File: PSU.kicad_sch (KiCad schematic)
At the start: 11 parts, among them J1 Mini USB Female, J2 Battery Connector, U3 AMS1117-3.3

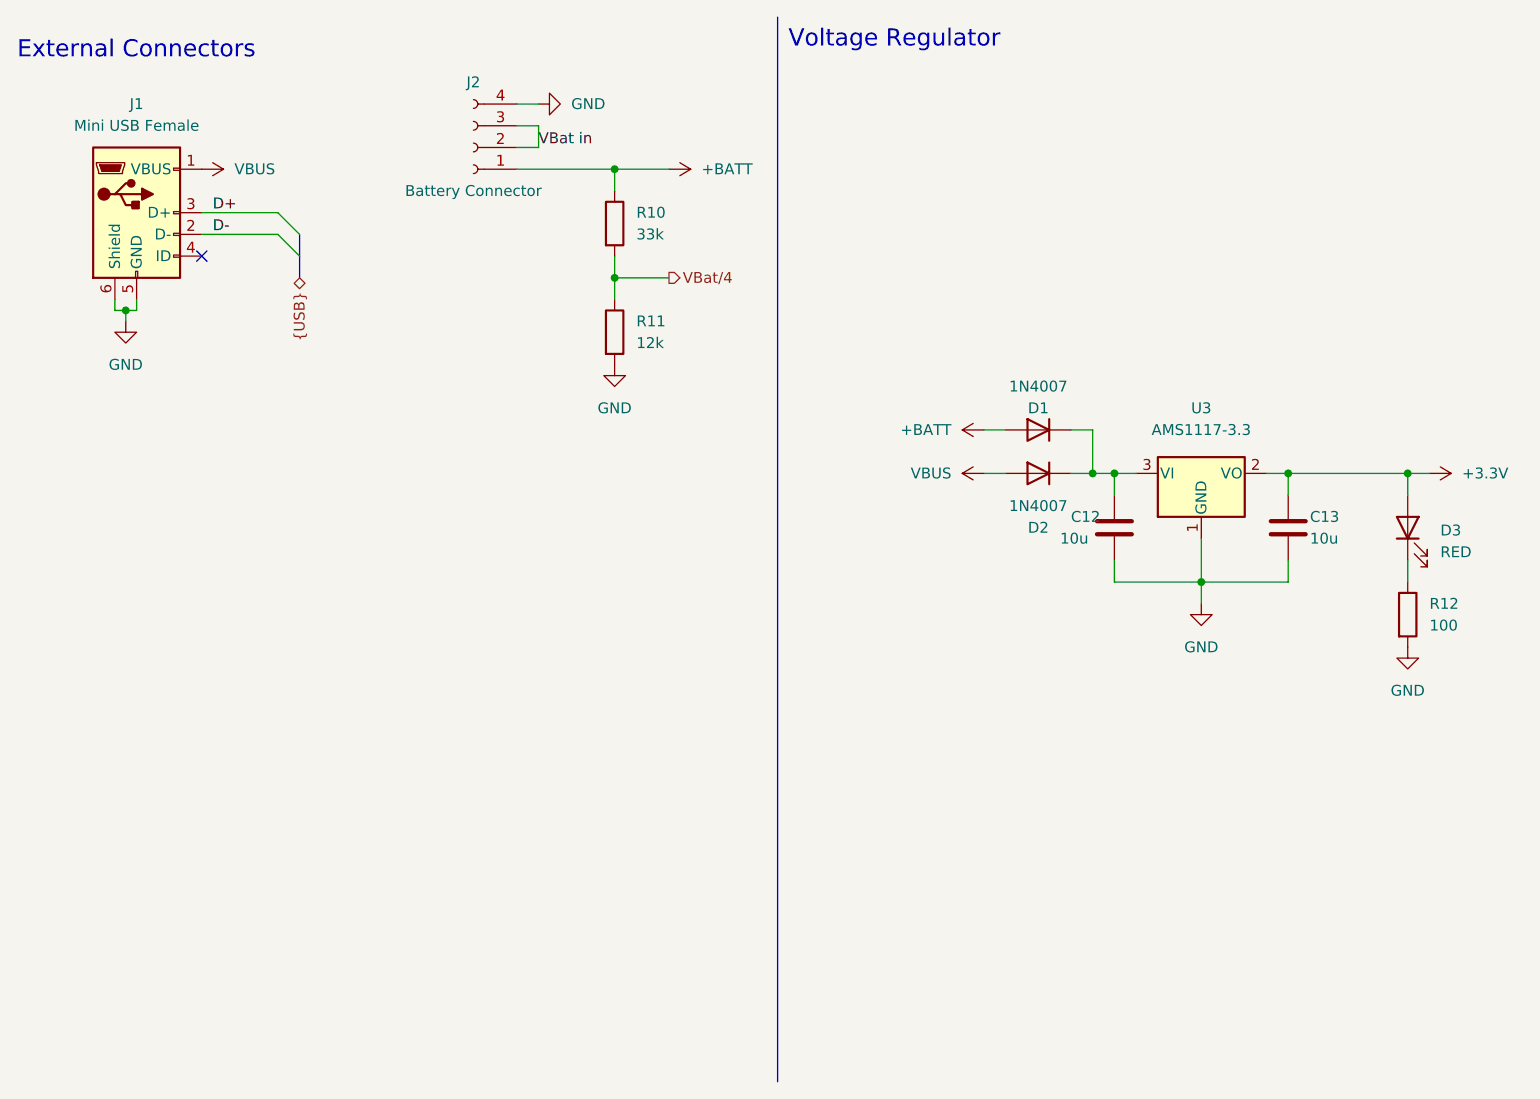
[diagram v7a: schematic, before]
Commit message: Added polyfuse
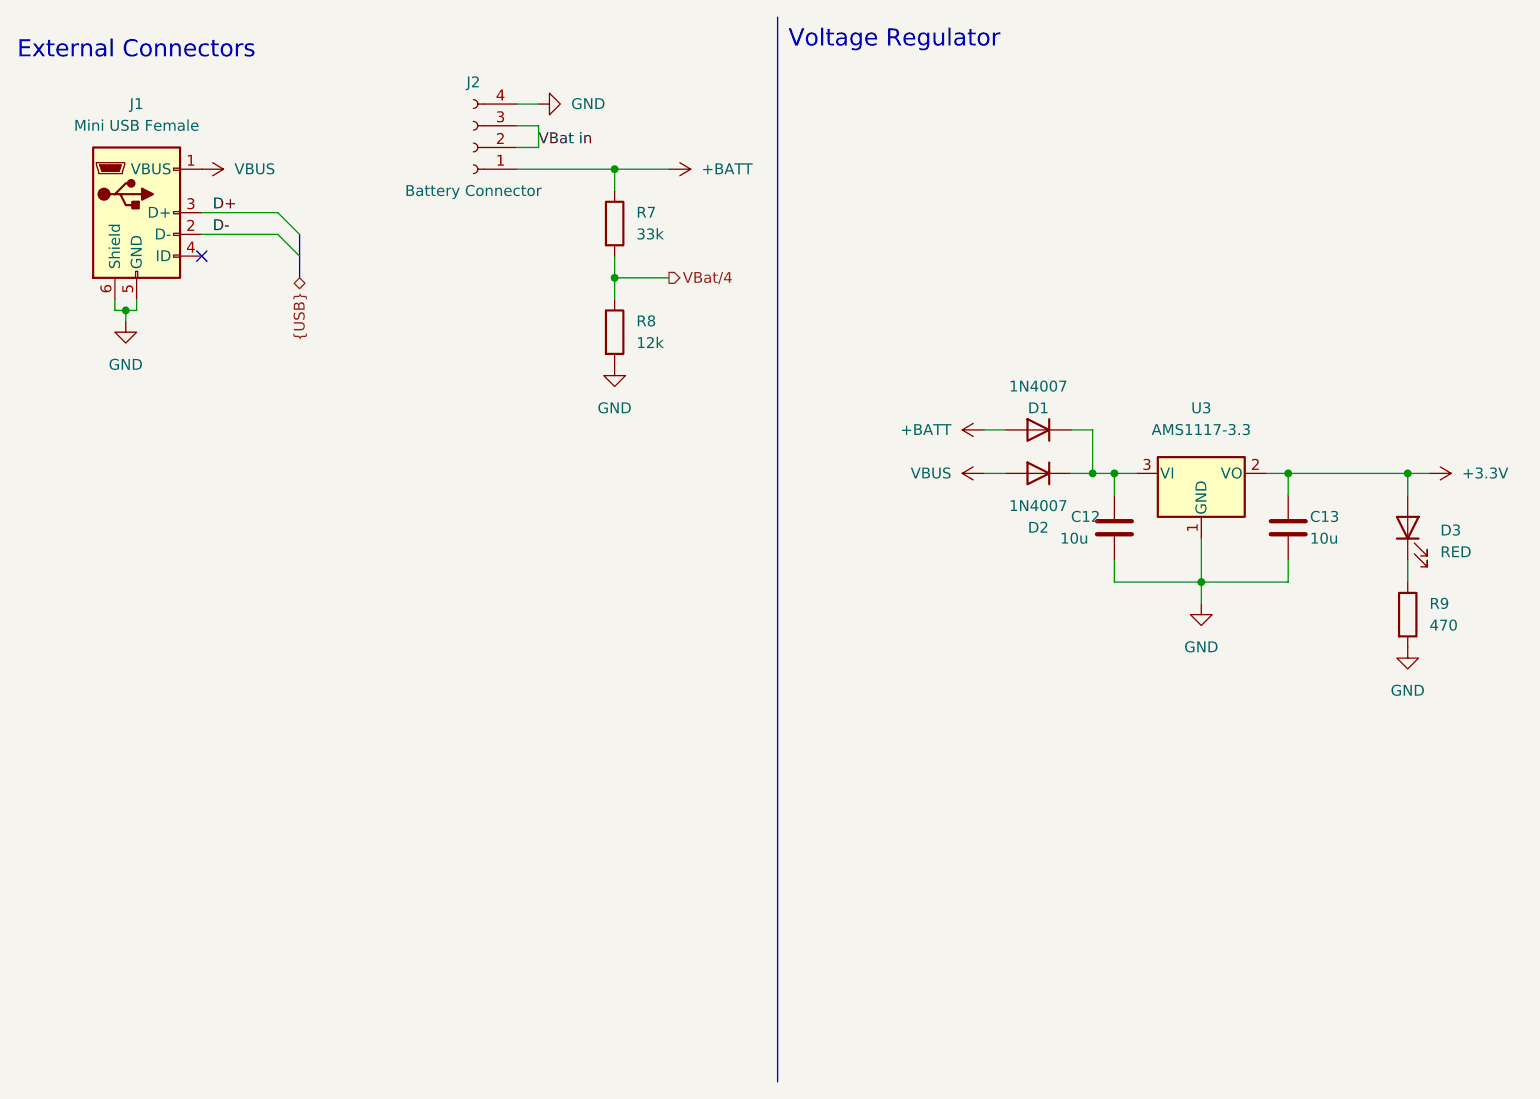
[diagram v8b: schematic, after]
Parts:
- D3: footprint LED_THT:LED_D3.0mm -> LED_SMD:LED_0603_1608Metric
- R9: renamed from R12; value 100 -> 470
- renumbered R10 to R7, R11 to R8
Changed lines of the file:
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@@
   (symbol (lib_id "power:+3.3V") (at 177.8 64.77 270) (unit 1)
     (in_bom yes) (on_board yes) (fields_autoplaced)
-    (property "Reference" "#PWR027" (id 0) (at 173.99 64.77 0)
+    (property "Reference" "#PWR025" (id 0) (at 173.99 64.77 0)
       (effects (font (size 1.27 1.27)) hide)
     )
@@
       (effects (font (size 1.27 1.27)) (justify right))
     )
-    (property "Footprint" "LED_THT:LED_D3.0mm" (id 2) (at 175.26 71.12 0)
+    (property "Footprint" "LED_SMD:LED_0603_1608Metric" (id 2) (at 175.26 71.12 0)
       (effects (font (size 1.27 1.27)) hide)
     )
@@
   (symbol (lib_id "Device:R") (at 82.55 35.56 0) (unit 1)
     (in_bom yes) (on_board yes) (fields_autoplaced)
-    (property "Reference" "R10" (id 0) (at 85.09 34.2899 0)
+    (property "Reference" "R7" (id 0) (at 85.09 34.2899 0)
       (effects (font (size 1.27 1.27)) (justify left))
     )
@@
   (symbol (lib_id "power:+BATT") (at 88.9 29.21 270) (unit 1)
     (in_bom yes) (on_board yes) (fields_autoplaced)
-    (property "Reference" "#PWR022" (id 0) (at 85.09 29.21 0)
+    (property "Reference" "#PWR020" (id 0) (at 85.09 29.21 0)
       (effects (font (size 1.27 1.27)) hide)
     )
@@
   (symbol (lib_id "power:GND") (at 175.26 85.09 0) (unit 1)
     (in_bom yes) (on_board yes) (fields_autoplaced)
-    (property "Reference" "#PWR026" (id 0) (at 175.26 91.44 0)
+    (property "Reference" "#PWR024" (id 0) (at 175.26 91.44 0)
       (effects (font (size 1.27 1.27)) hide)
     )
@@
   (symbol (lib_id "power:GND") (at 25.4 46.99 0) (unit 1)
     (in_bom yes) (on_board yes) (fields_autoplaced)
-    (property "Reference" "#PWR018" (id 0) (at 25.4 53.34 0)
+    (property "Reference" "#PWR016" (id 0) (at 25.4 53.34 0)
       (effects (font (size 1.27 1.27)) hide)
     )
@@
   (symbol (lib_id "power:VBUS") (at 34.29 29.21 270) (unit 1)
     (in_bom yes) (on_board yes) (fields_autoplaced)
-    (property "Reference" "#PWR019" (id 0) (at 30.48 29.21 0)
+    (property "Reference" "#PWR017" (id 0) (at 30.48 29.21 0)
       (effects (font (size 1.27 1.27)) hide)
     )
@@
   (symbol (lib_id "Device:R") (at 82.55 48.26 0) (unit 1)
     (in_bom yes) (on_board yes) (fields_autoplaced)
-    (property "Reference" "R11" (id 0) (at 85.09 46.9899 0)
+    (property "Reference" "R8" (id 0) (at 85.09 46.9899 0)
       (effects (font (size 1.27 1.27)) (justify left))
     )
@@
   (symbol (lib_id "Device:R") (at 175.26 81.28 0) (unit 1)
     (in_bom yes) (on_board yes) (fields_autoplaced)
-    (property "Reference" "R12" (id 0) (at 177.8 80.0099 0)
-      (effects (font (size 1.27 1.27)) (justify left))
-    )
-    (property "Value" "100" (id 1) (at 177.8 82.5499 0)
+    (property "Reference" "R9" (id 0) (at 177.8 80.0099 0)
+      (effects (font (size 1.27 1.27)) (justify left))
+    )
+    (property "Value" "470" (id 1) (at 177.8 82.5499 0)
       (effects (font (size 1.27 1.27)) (justify left))
     )
@@
   (symbol (lib_id "power:GND") (at 82.55 52.07 0) (unit 1)
     (in_bom yes) (on_board yes) (fields_autoplaced)
-    (property "Reference" "#PWR021" (id 0) (at 82.55 58.42 0)
+    (property "Reference" "#PWR019" (id 0) (at 82.55 58.42 0)
       (effects (font (size 1.27 1.27)) hide)
     )
@@
   (symbol (lib_id "power:VBUS") (at 125.73 64.77 90) (mirror x) (unit 1)
     (in_bom yes) (on_board yes) (fields_autoplaced)
-    (property "Reference" "#PWR024" (id 0) (at 129.54 64.77 0)
+    (property "Reference" "#PWR022" (id 0) (at 129.54 64.77 0)
       (effects (font (size 1.27 1.27)) hide)
     )
@@
   (symbol (lib_id "power:GND") (at 151.13 80.01 0) (unit 1)
     (in_bom yes) (on_board yes) (fields_autoplaced)
-    (property "Reference" "#PWR025" (id 0) (at 151.13 86.36 0)
+    (property "Reference" "#PWR023" (id 0) (at 151.13 86.36 0)
       (effects (font (size 1.27 1.27)) hide)
     )
@@
   (symbol (lib_id "power:GND") (at 73.66 21.59 90) (unit 1)
     (in_bom yes) (on_board yes) (fields_autoplaced)
-    (property "Reference" "#PWR020" (id 0) (at 80.01 21.59 0)
+    (property "Reference" "#PWR018" (id 0) (at 80.01 21.59 0)
       (effects (font (size 1.27 1.27)) hide)
     )
@@
   (symbol (lib_id "power:+BATT") (at 125.73 59.69 90) (mirror x) (unit 1)
     (in_bom yes) (on_board yes) (fields_autoplaced)
-    (property "Reference" "#PWR023" (id 0) (at 129.54 59.69 0)
-      (effects (font (size 1.27 1.27)) hide)
-    )
+    (property "Reference" "#PWR021" (id 0) (at 129.54 59.69 0)
+      (effects (font (size 1.27 1.27)) hide)
+    )
